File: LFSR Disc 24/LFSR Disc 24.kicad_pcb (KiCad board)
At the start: 2 copper layers, 152.4 x 152.4 mm, 51 parts, among them U201 74HC164, U202 74HC164, U203 74HC164

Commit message: Filling things out a little
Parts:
- added C401: 10u, Capacitor_THT:CP_Radial_D4.0mm_P1.50mm, F.Cu at (74.7, 111.8)
- added C402: 0.1u, Capacitor_THT:C_Disc_D4.3mm_W1.9mm_P5.00mm, F.Cu at (78.8, 92.7)
- added C403: 0.01u, Capacitor_THT:C_Disc_D3.4mm_W2.1mm_P2.50mm, F.Cu at (85.1, 108.0)
- added R401: 10k, Resistor_THT:R_Axial_DIN0207_L6.3mm_D2.5mm_P7.62mm_Horizontal, F.Cu at (54.6, 92.7)
- added R402: 10k, Resistor_THT:R_Axial_DIN0207_L6.3mm_D2.5mm_P7.62mm_Horizontal, F.Cu at (54.6, 100.3)
- added R403: 1k, Resistor_THT:R_Axial_DIN0207_L6.3mm_D2.5mm_P7.62mm_Horizontal, F.Cu at (54.6, 108.0)
- added RV401: R_Potentiometer, Potentiometer_THT:Potentiometer_Piher_PT-10-V10_Vertical, F.Cu at (57.2, 120.8)
- added U401: LM555xN, Package_DIP:DIP-8_W7.62mm, F.Cu at (77.5, 96.5)
- added U501: 74HC86, Package_DIP:DIP-14_W7.62mm_Socket, F.Cu at (112.7, 97.8)
- added U502: 74LS125, Package_DIP:DIP-14_W7.62mm_Socket, F.Cu at (124.5, 97.8)
- R301, R302, R303, R304, R305, R306, R307, R308, R309, R310, R311, R312, R313, R314, R315, R316, R317, R318, R319, R320, R321, R322, R323, R324: value R -> 4k7
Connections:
- U201 pad 8: unconnected-(U201-CP-Pad8) -> /Shift Clock/CLK
- U202 pad 8: unconnected-(U202-CP-Pad8) -> /Shift Clock/CLK
- U203 pad 10: unconnected-(U203-Q4-Pad10) -> /LED Output/LED21
- U203 pad 11: unconnected-(U203-Q5-Pad11) -> /LED Output/LED22
- U203 pad 12: unconnected-(U203-Q6-Pad12) -> /LED Output/LED23
- U203 pad 13: unconnected-(U203-Q7-Pad13) -> /LED Output/LED24
- U203 pad 3: unconnected-(U203-Q0-Pad3) -> /LED Output/LED17
- U203 pad 4: unconnected-(U203-Q1-Pad4) -> /LED Output/LED18
- U203 pad 5: unconnected-(U203-Q2-Pad5) -> /LED Output/LED19
- U203 pad 6: unconnected-(U203-Q3-Pad6) -> /LED Output/LED20
- U203 pad 8: unconnected-(U203-CP-Pad8) -> /Shift Clock/CLK

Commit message: More things assembling
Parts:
- added C201: 0.1u, Capacitor_THT:C_Disc_D4.3mm_W1.9mm_P5.00mm, F.Cu at (139.7, 63.5)
- added C202: 0.1u, Capacitor_THT:C_Disc_D4.3mm_W1.9mm_P5.00mm, F.Cu at (104.1, 152.4)
- added C203: 0.1u, Capacitor_THT:C_Disc_D4.3mm_W1.9mm_P5.00mm, F.Cu at (63.5, 63.5)
- added R501: 100k, Resistor_THT:R_Axial_DIN0207_L6.3mm_D2.5mm_P7.62mm_Horizontal, F.Cu at (96.5, 107.5)
- added R502: 100k, Resistor_THT:R_Axial_DIN0207_L6.3mm_D2.5mm_P7.62mm_Horizontal, F.Cu at (96.5, 111.5)
- added R503: 100k, Resistor_THT:R_Axial_DIN0207_L6.3mm_D2.5mm_P7.62mm_Horizontal, F.Cu at (96.5, 115.6)
- added SW501: SW_SPST, Button_Switch_THT:SW_PUSH_6mm, F.Cu at (98.9, 81.9)
- added SW502: SW_SPST, Button_Switch_THT:SW_PUSH_6mm, F.Cu at (98.9, 73.3)
- U502: value 74LS125 -> 74HCT125
- moved U202 17.0 mm to (105.4, 147.3), turned to 180 degrees
- moved U201 8.13 mm to (129.5, 73.7), turned to -45 degrees
- moved U203 5.24 mm to (73.7, 73.7), turned to 45 degrees
- moved U501 0.95 mm to (111.8, 97.8)
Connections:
- D309 pad 2: unconnected-(D309-A-Pad2) -> /LED Output/LED9
- D310 pad 2: unconnected-(D310-A-Pad2) -> /LED Output/LED10
- D311 pad 2: unconnected-(D311-A-Pad2) -> /LED Output/LED11
- D312 pad 2: unconnected-(D312-A-Pad2) -> /LED Output/LED12
- D313 pad 2: unconnected-(D313-A-Pad2) -> /LED Output/LED13
- D314 pad 2: unconnected-(D314-A-Pad2) -> /LED Output/LED14
- D315 pad 2: unconnected-(D315-A-Pad2) -> /LED Output/LED15
- U201 pad 1: unconnected-(U201-DSA-Pad1) -> /Shift Registers/Feedback/NXTBIT
- U201 pad 2: unconnected-(U201-DSB-Pad2) -> /Shift Registers/Feedback/NXTBIT
- U502 pad 10: unconnected-(U502-Pad10) -> /Shift Registers/Feedback/~{FEEDBACK}
- U502 pad 5: unconnected-(U502-Pad5) -> Net-(SW502-B)
- U502 pad 8: unconnected-(U502-Pad8) -> /Shift Registers/Feedback/~{MANUAL}
- U502 pad 9: unconnected-(U502-Pad9) -> +5V

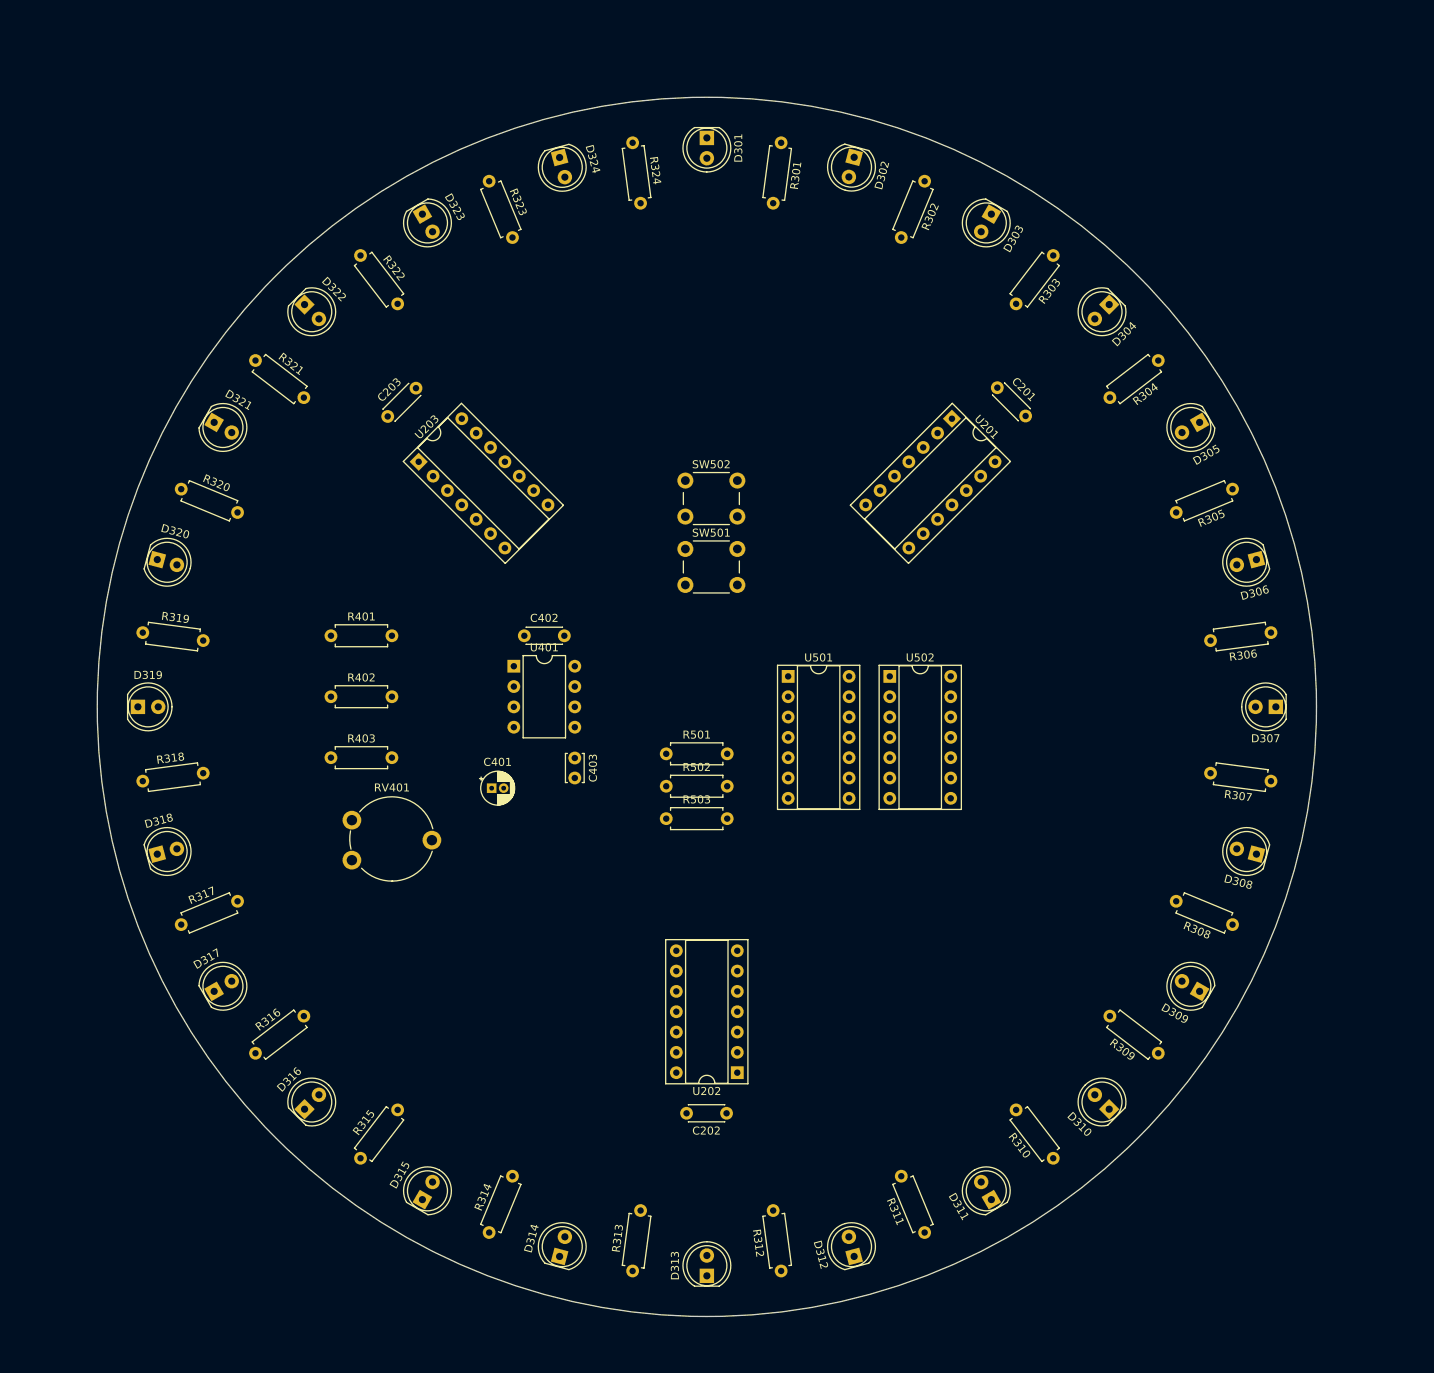
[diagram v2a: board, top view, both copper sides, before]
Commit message: Board layout and schematic tweaks
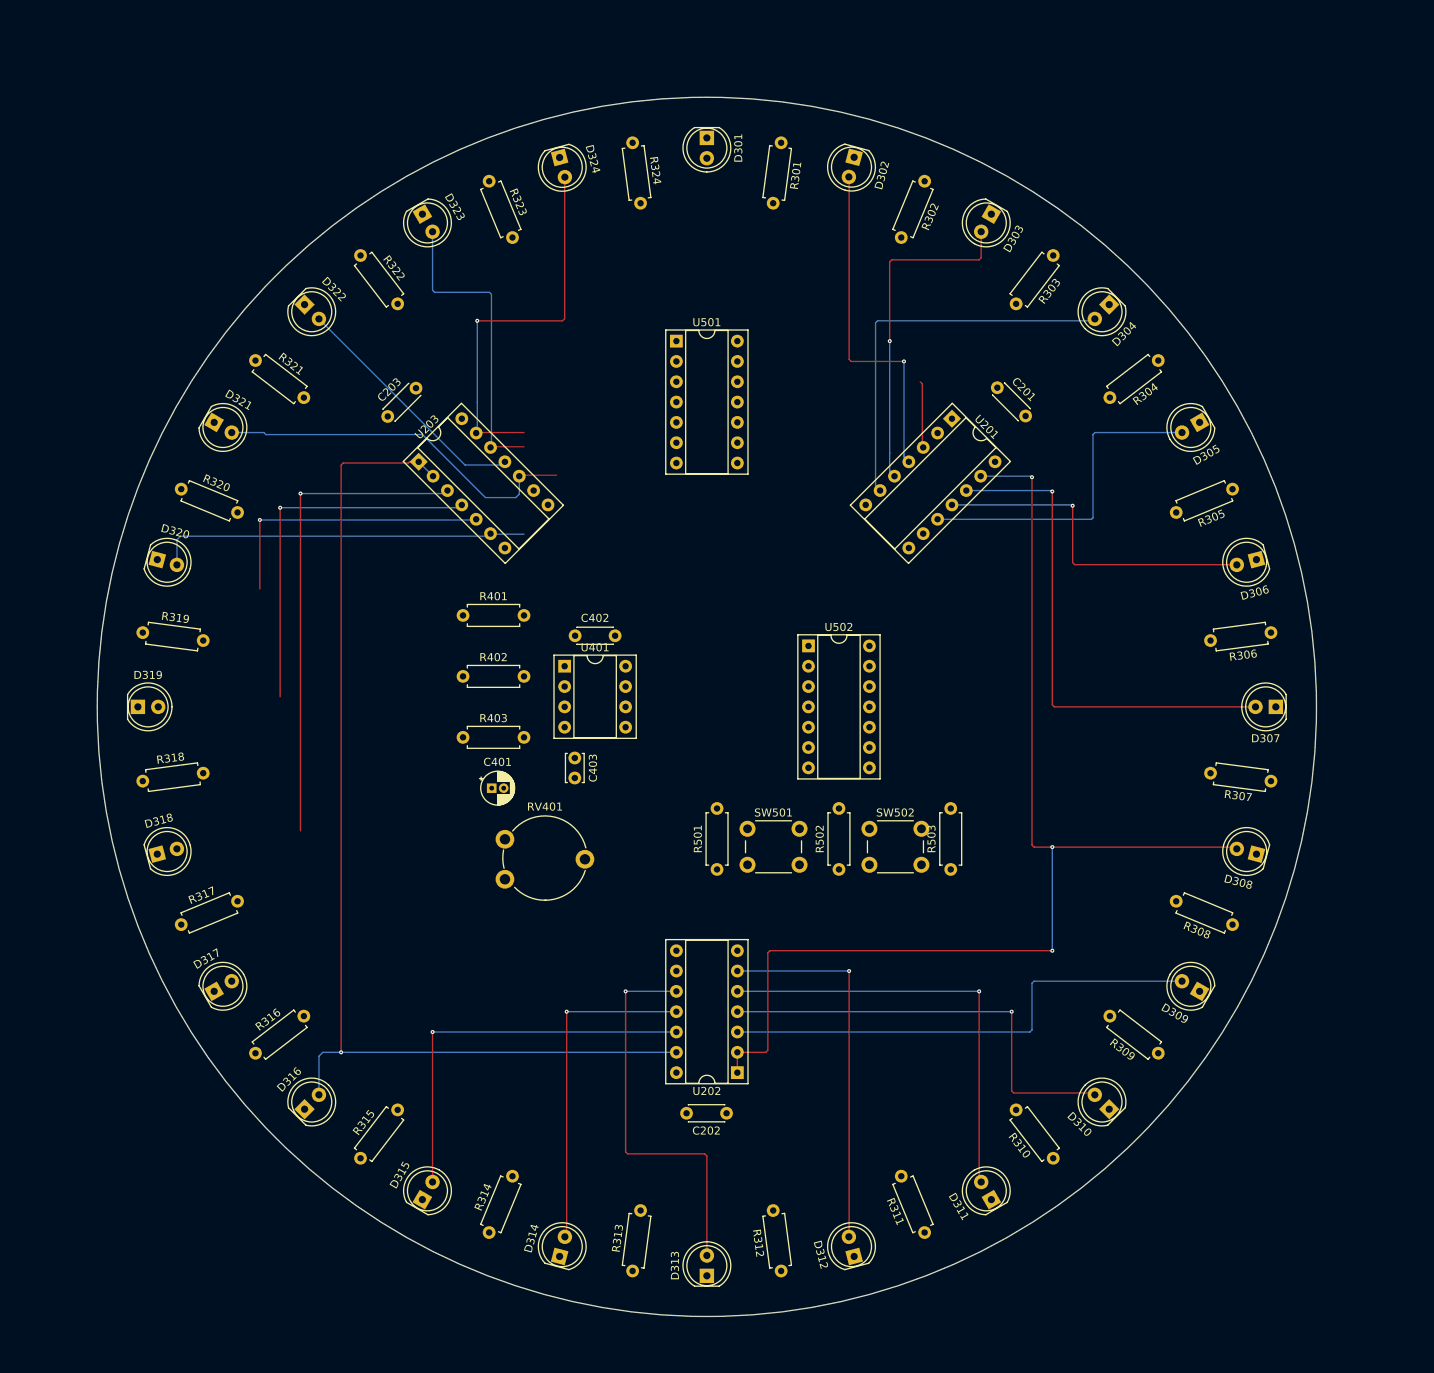
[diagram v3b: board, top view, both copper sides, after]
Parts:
- U401: footprint Package_DIP:DIP-8_W7.62mm -> Package_DIP:DIP-8_W7.62mm_Socket
- moved SW502 49.2 mm to (121.9, 116.8)
- moved U501 44.2 mm to (97.8, 55.9)
- moved R503 36.1 mm to (132.1, 121.9), turned to 90 degrees
- moved SW501 35.8 mm to (106.7, 116.8)
- moved R502 24.0 mm to (118.1, 121.9), turned to 90 degrees
- moved RV401 19.3 mm to (76.4, 123.2)
- moved R403 16.7 mm to (71.1, 105.4)
- moved R401 16.7 mm to (71.1, 90.2)
- moved R402 16.7 mm to (71.1, 97.8)
- moved R501 15.8 mm to (102.9, 121.9), turned to 90 degrees
- moved U502 10.9 mm to (114.3, 94.0)
- moved C402 6.35 mm to (85.1, 92.7)
- moved U401 6.35 mm to (83.8, 96.5)
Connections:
- D317 pad 2: unconnected-(D317-A-Pad2) -> /LED Output/LED17
- D318 pad 2: unconnected-(D318-A-Pad2) -> /LED Output/LED18
- D319 pad 2: unconnected-(D319-A-Pad2) -> /LED Output/LED19
- D320 pad 2: unconnected-(D320-A-Pad2) -> /LED Output/LED20
- D321 pad 2: unconnected-(D321-A-Pad2) -> /LED Output/LED21
- D322 pad 2: unconnected-(D322-A-Pad2) -> /LED Output/LED22
- D323 pad 2: unconnected-(D323-A-Pad2) -> /LED Output/LED23
- D324 pad 2: unconnected-(D324-A-Pad2) -> /LED Output/LED24
- U501 pad 1: /Shift Registers/Feedback/IN0 -> /LED Output/LED24
- U501 pad 2: /Shift Registers/Feedback/IN1 -> /LED Output/LED23
- U501 pad 3: Net-(U501-Pad3) -> Net-(U501-Pad10)
- U501 pad 4: /Shift Registers/Feedback/IN2 -> /LED Output/LED21
- U501 pad 5: /Shift Registers/Feedback/IN3 -> /LED Output/LED20
- U501 pad 6: Net-(U501-Pad10) -> Net-(U501-Pad6)
- U501 pad 9: Net-(U501-Pad3) -> Net-(U501-Pad6)
- U502 pad 1: unconnected-(U502-Pad1) -> /Shift Registers/Feedback/~{FEEDBACK}
- U502 pad 11: unconnected-(U502-Pad11) -> /Shift Registers/Feedback/NXTBIT
- U502 pad 12: unconnected-(U502-Pad12) -> Net-(SW502-B)
- U502 pad 13: unconnected-(U502-Pad13) -> /Shift Registers/Feedback/~{MANUAL}
- U502 pad 5: Net-(SW502-B) -> unconnected-(U502-Pad5)
- U502 pad 6: /Shift Registers/Feedback/NXTBIT -> unconnected-(U502-Pad6)
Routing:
- net /LED Output/LED8: track 0.00 -> 145.5 mm, vias 0 -> 3
- net /LED Output/LED16: track 0.00 -> 135.9 mm, vias 0 -> 1
- net /LED Output/LED7: track 0.00 -> 63.0 mm, vias 0 -> 1
- net /LED Output/LED9: track 0.00 -> 61.6 mm
- net /LED Output/LED17: track 0.00 -> 60.7 mm, vias 0 -> 1
- net /LED Output/LED10: track 0.00 -> 54.8 mm, vias 0 -> 1
- net /LED Output/LED11: track 0.00 -> 54.2 mm, vias 0 -> 1
- net /LED Output/LED13: track 0.00 -> 49.2 mm, vias 0 -> 1
- net /LED Output/LED15: track 0.00 -> 49.2 mm, vias 0 -> 1
- net /LED Output/LED24: track 0.00 -> 48.8 mm, vias 0 -> 1
- net /LED Output/LED4: track 0.00 -> 48.8 mm
- net /LED Output/LED12: track 0.00 -> 47.2 mm, vias 0 -> 1
- net /LED Output/LED20: track 0.00 -> 46.9 mm
- net /LED Output/LED18: track 0.00 -> 46.5 mm, vias 0 -> 1
- net /LED Output/LED21: track 0.00 -> 46.5 mm
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
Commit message: Final routing
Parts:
- added J101: USB_A, Connector_USB:USB_A_Molex_67643_Horizontal, B.Cu at (104.8, 99.1)
- added J102: Conn_01x02_Pin, Connector_PinHeader_2.54mm:PinHeader_1x02_P2.54mm_Vertical, B.Cu at (100.3, 92.7)
- added J401: Conn_01x02_Pin, Connector_PinHeader_2.54mm:PinHeader_1x02_P2.54mm_Vertical, F.Cu at (82.5, 87.6)
- C401: value 10u -> C_Polarized_Small
- moved RV401 22.3 mm to (64.8, 104.1)
- moved R403 7.41 mm to (67.3, 111.8)
- moved C401 5.89 mm to (80.0, 109.2), turned to -90 degrees
- moved R402 5.39 mm to (67.3, 94.0)
- moved C402 4.05 mm to (81.3, 94.0)
- moved U401 4.02 mm to (80.0, 97.8)
- moved R401 3.81 mm to (67.3, 90.2)
- moved C403 2.82 mm to (87.6, 109.2)
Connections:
- R401 pad 1: +5V -> /Shift Clock/DIVIDER
- R401 pad 2: /Shift Clock/DIVIDER -> +5V
- RV401 pad 1: Net-(R402-Pad2) -> /Shift Clock/TRTHR
- RV401 pad 3: /Shift Clock/TRTHR -> Net-(R402-Pad2)
- U201 pad 9: unconnected-(U201-~{MR}-Pad9) -> +5V
- U202 pad 9: unconnected-(U202-~{MR}-Pad9) -> +5V
- U203 pad 9: unconnected-(U203-~{MR}-Pad9) -> +5V
- U501 pad 12: unconnected-(U501-Pad12) -> GND
- U501 pad 13: unconnected-(U501-Pad13) -> GND
- U502 pad 4: unconnected-(U502-Pad4) -> GND
- U502 pad 5: unconnected-(U502-Pad5) -> GND
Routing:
- net /Shift Clock/CLK: track 0.00 -> 142.1 mm
- net /LED Output/LED1: track 8.36 -> 62.5 mm
- net /Shift Registers/Feedback/~{FEEDBACK}: track 0.00 -> 53.4 mm
- net /Shift Registers/Feedback/NXTBIT: track 0.00 -> 51.5 mm
- net /Shift Clock/DIVIDER: track 0.00 -> 46.2 mm
- net /Shift Registers/Feedback/~{MANUAL}: track 0.00 -> 43.7 mm
- net /Shift Clock/TRTHR: track 0.00 -> 42.3 mm
- net Net-(SW502-B): track 0.00 -> 38.9 mm, vias 0 -> 1
- net Net-(U501-Pad8): track 0.00 -> 34.0 mm
- net /LED Output/LED20: track 46.9 -> 79.6 mm
- net /LED Output/LED18: track 46.5 -> 78.3 mm
- net /LED Output/LED24: track 48.8 -> 79.0 mm
- net /LED Output/LED23: track 38.3 -> 67.7 mm
- net /LED Output/LED19: track 35.7 -> 63.0 mm
- net /LED Output/LED17: track 60.7 -> 87.9 mm
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- added copper zone on B.Cu, net +5V
- added copper zone on F.Cu, net GND
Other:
- board text added: "+5v"
- board text added: "CLK"
- board text added: "GND"
- board text added: "RGE2023"

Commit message: Update some values
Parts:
- C401: value C_Polarized_Small -> 10u
- R402: value 10k -> 2k2
- RV401: value R_Potentiometer -> 100k
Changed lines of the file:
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@@
         (effects (font (size 1 1) (thickness 0.15)))
     )
-    (fp_text value "R_Potentiometer" (at 5 3.75) (layer "F.Fab")
+    (fp_text value "100k" (at 5 3.75) (layer "F.Fab")
         (effects (font (size 1 1) (thickness 0.15)))
     )
@@
         (effects (font (size 1 1) (thickness 0.15)))
     )
-    (fp_text value "10k" (at 3.81 2.37) (layer "F.Fab")
+    (fp_text value "2k2" (at 3.81 2.37) (layer "F.Fab")
         (effects (font (size 1 1) (thickness 0.15)))
     )
@@
         (effects (font (size 1 1) (thickness 0.15)))
     )
-    (fp_text value "C_Polarized_Small" (at 0.75 3.25 90) (layer "F.Fab")
+    (fp_text value "10u" (at 0.75 3.25 90) (layer "F.Fab")
         (effects (font (size 1 1) (thickness 0.15)))
     )

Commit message: Holes, silkscreen....
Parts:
- added H101: MountingHole, MountingHole:MountingHole_2.7mm_M2.5_ISO7380, F.Cu at (59.7, 83.8)
- added H102: MountingHole, MountingHole:MountingHole_2.7mm_M2.5_ISO7380, F.Cu at (143.5, 83.8)
- added H103: MountingHole, MountingHole:MountingHole_2.7mm_M2.5_ISO7380, F.Cu at (59.7, 119.4)
- added H104: MountingHole, MountingHole:MountingHole_2.7mm_M2.5_ISO7380, F.Cu at (143.5, 119.4)
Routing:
- net /LED Output/LED8: track 145.5 -> 149.5 mm, vias 3 -> 2
- net /LED Output/LED7: track 63.0 -> 63.3 mm, vias 1 -> 0
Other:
- board text added: "24-bit LFSR Taps 20, 21, 23, 24"
- board text added: "JLCJLCJLCJLC"
